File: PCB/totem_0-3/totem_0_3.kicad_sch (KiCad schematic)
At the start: 93 parts, among them J1 MJ-4PP-9, J2 MJ-4PP-9, J3 Conn_01x12_Socket, J4 Conn_01x03_Socket, SW1 SW_Push_45deg, SW10 SW_Push_45deg, SW11 SW_Push_45deg, SW12 SW_Push_45deg, SW13 SW_Push_45deg, SW14 SW_Push_45deg, SW15 SW_Push_45deg, SW16 SW_Push_45deg, SW17 SW_Push_45deg, SW18 SW_Push_45deg, SW19 SW_Push_45deg, SW2 SW_Push_45deg, SW20 SW_Push, SW21 SW_SPDT, SW22 SW_SPDT, SW23 SW_Push, SW24 SW_Push_45deg, SW25 SW_Push_45deg, SW26 SW_Push_45deg, SW27 SW_Push_45deg, SW28 SW_Push_45deg, SW29 SW_Push_45deg, SW3 SW_Push_45deg, SW30 SW_Push_45deg, SW31 SW_Push_45deg, SW32 SW_Push_45deg, SW33 SW_Push_45deg, SW34 SW_Push_45deg, SW35 SW_Push_45deg, SW36 SW_Push_45deg, SW37 SW_Push_45deg, SW38 SW_Push_45deg, SW39 SW_Push_45deg, SW4 SW_Push_45deg, SW40 SW_Push_45deg, SW41 SW_Push_45deg, SW42 SW_Push_45deg, SW5 SW_Push_45deg, SW6 SW_Push_45deg, SW7 SW_Push_45deg, SW8 SW_Push_45deg, SW9 SW_Push_45deg, U1 xiao-ble, U2 74HC595, U3 xiao-ble

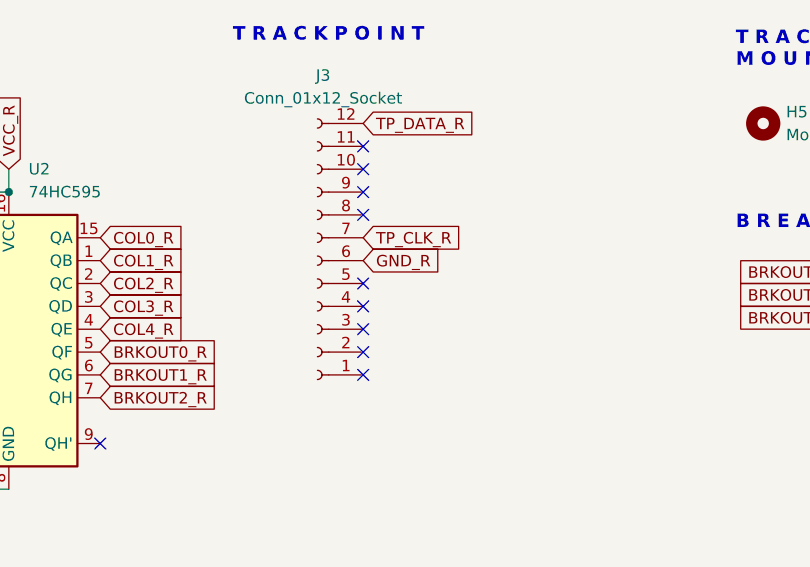
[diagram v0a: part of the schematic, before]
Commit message: sch: add VCC for trackpoint
Signed-off-by: Anant Thazhemadam <anant.thazhemadam@gmail.com>
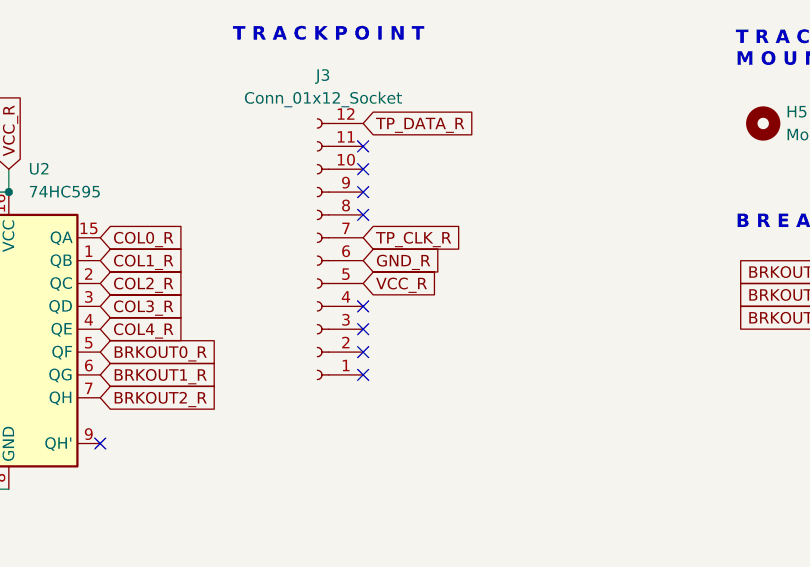
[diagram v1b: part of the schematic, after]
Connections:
- net VCC_R: now also J3.5 (Pin_5)
- no-connect marks 22 -> 21
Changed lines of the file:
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@@
-	)
-	(no_connect
-		(at 257.81 207.01)
 	)
 	(no_connect
@@
 			(effects
 				(font
+					(size 1.27 1.27)
+				)
+				(justify left)
+				(hide yes)
+			)
+		)
+	)
+	(global_label "VCC_R"
+		(shape input)
+		(at 257.81 207.01 0)
+		(fields_autoplaced yes)
+		(effects
+			(font
+				(size 1.27 1.27)
+			)
+			(justify left)
+		)
+		(property "Intersheetrefs" "${INTERSHEET_REFS}"
+			(at 266.0893 206.9306 0)
+			(effects
+				(font

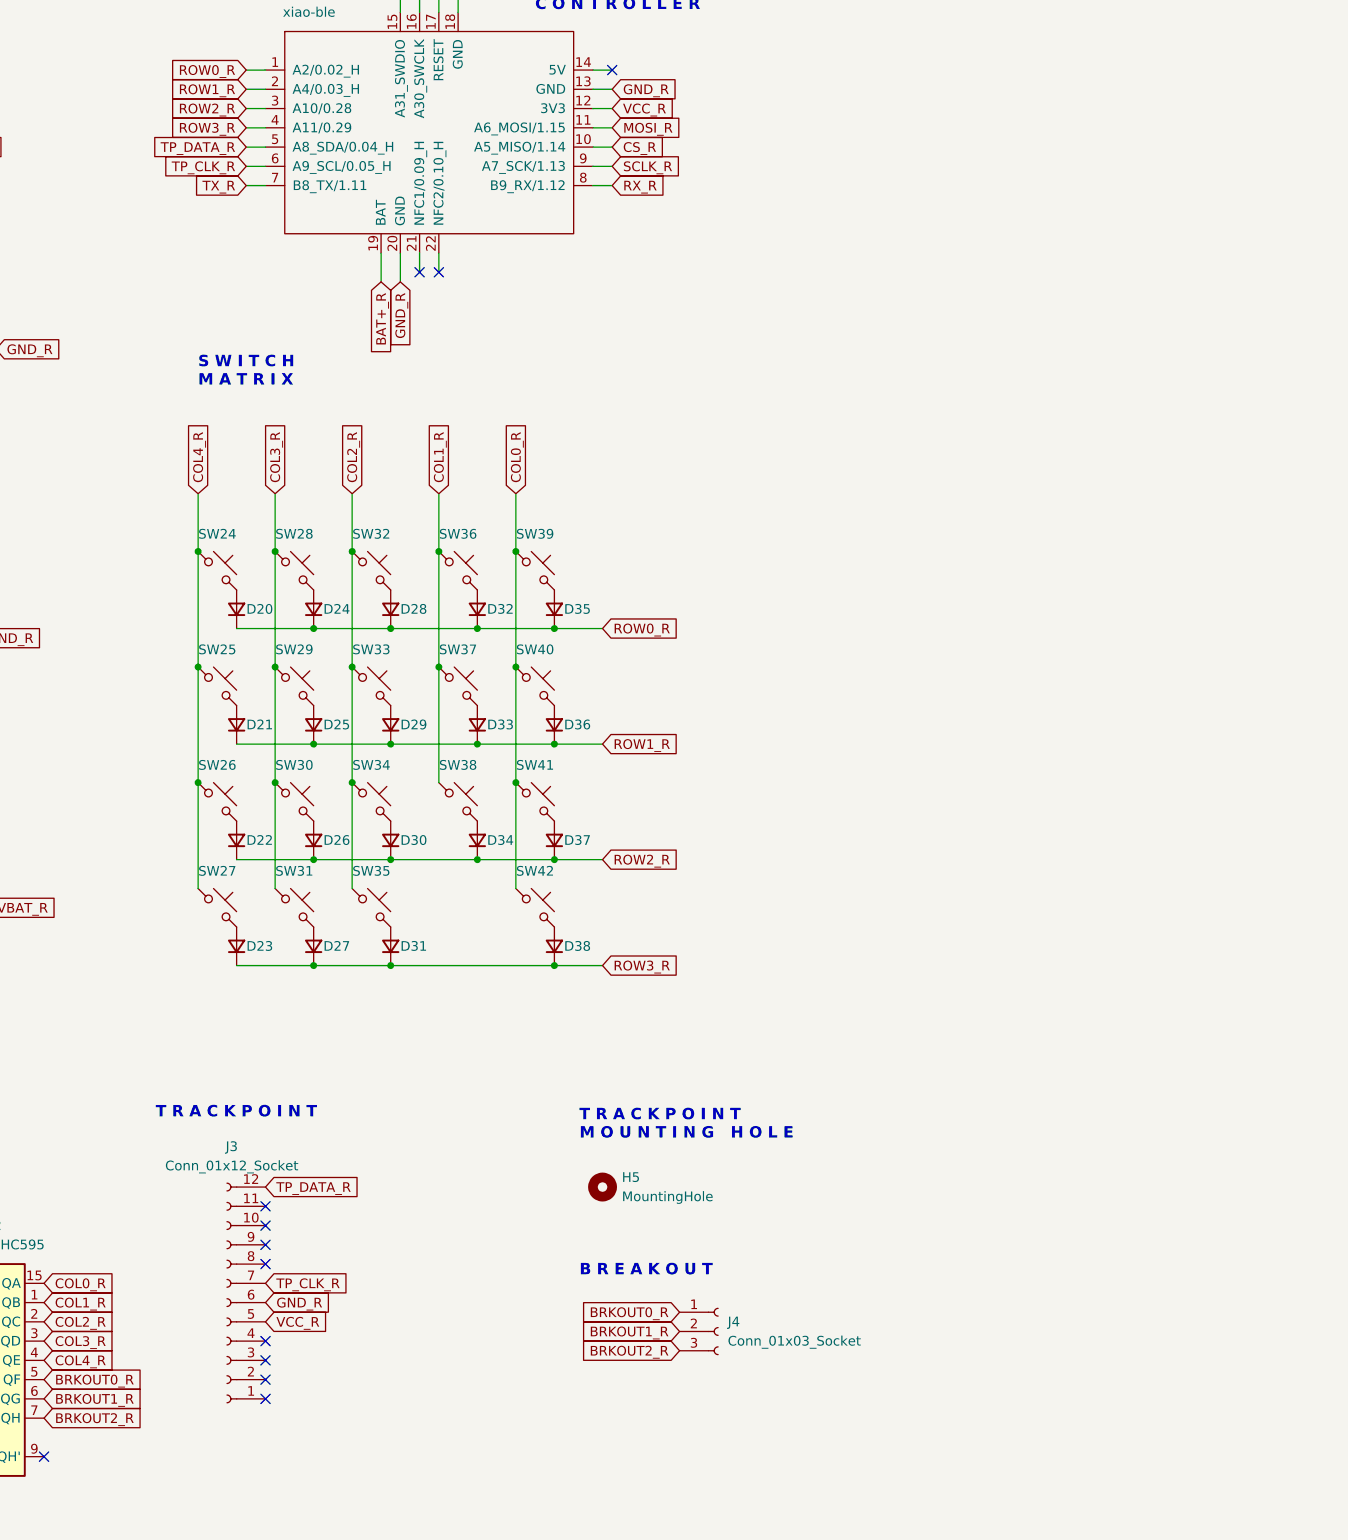
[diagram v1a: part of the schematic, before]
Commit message: sch: properly wire up trackpoint connector
Signed-off-by: Anant Thazhemadam <anant.thazhemadam@gmail.com>
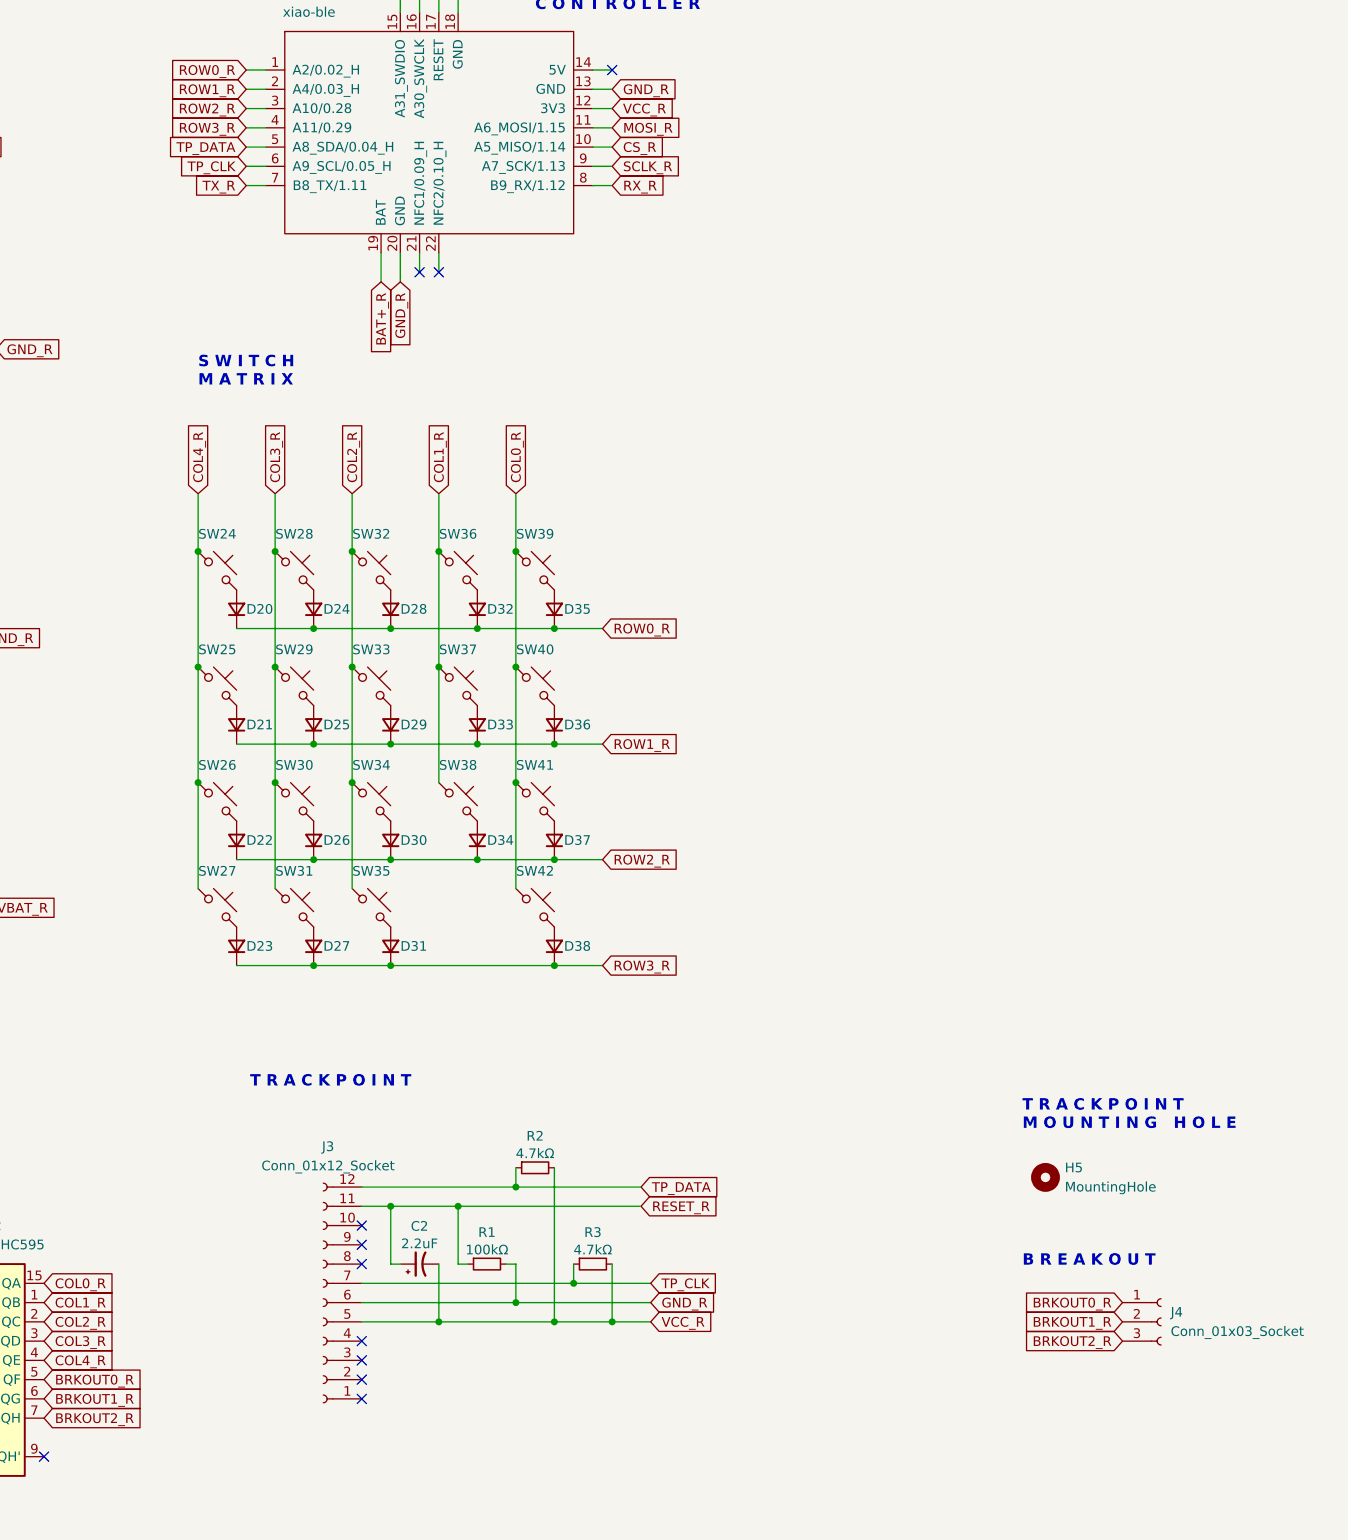
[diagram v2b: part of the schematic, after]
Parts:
- added C2: 2.2uF, Capacitor_SMD:C_0805_2012Metric_Pad1.18x1.45mm_HandSolder, symbol Device:CP1_Small
- added R1: 100kΩ, Resistor_SMD:R_0805_2012Metric_Pad1.20x1.40mm_HandSolder, symbol Device:R_Small
- added R2, R3: 4.7kΩ, Resistor_SMD:R_0805_2012Metric_Pad1.20x1.40mm_HandSolder, symbol Device:R_Small
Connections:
- net GND_R: now also R1.2
- net RESET_R: now also J3.11 (Pin_11), C2.1, R1.1
- net VCC_R: now also C2.2, R2.2, R3.2
- net TP_CLK_R renamed TP_CLK
- net TP_CLK: now also R3.1
- net TP_DATA_R renamed TP_DATA
- net TP_DATA: now also R2.1
- no-connect marks 21 -> 20
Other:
- moved on the sheet: H5, J3, J4

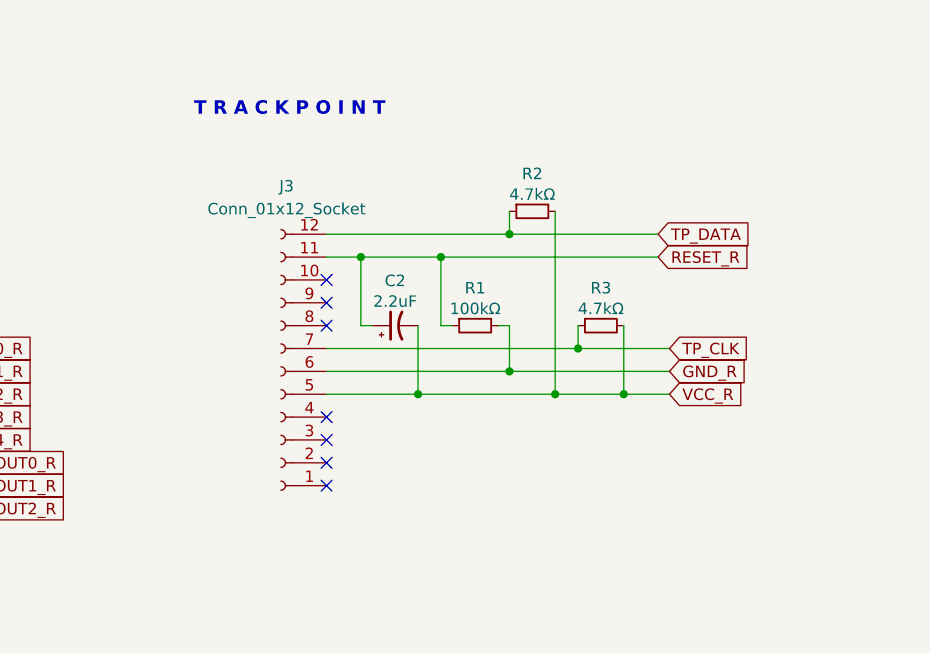
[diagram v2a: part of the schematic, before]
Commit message: sch: fix reset circuit for trackpoint
Signed-off-by: Anant Thazhemadam <anant.thazhemadam@gmail.com>
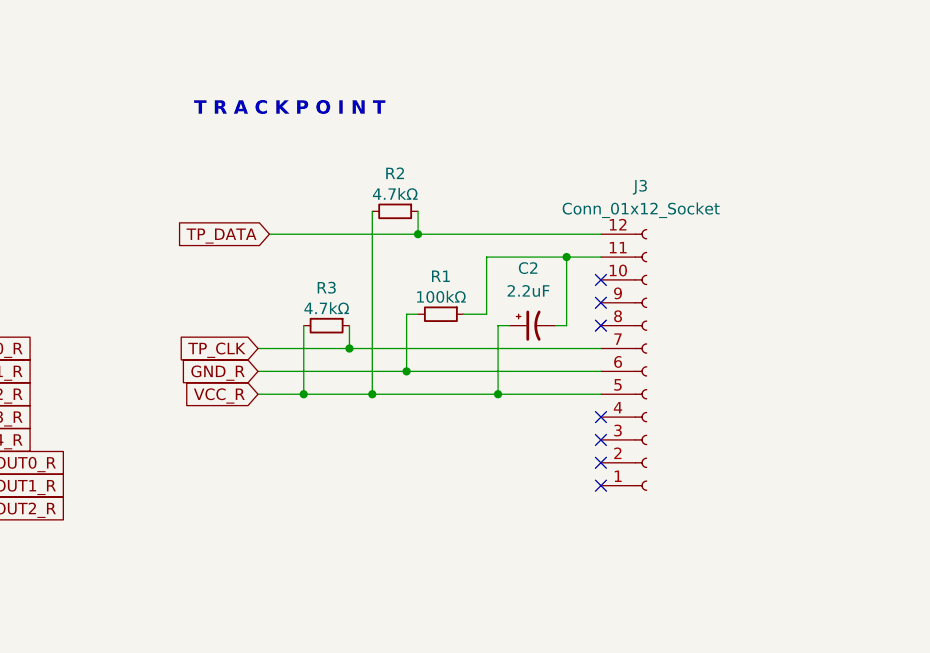
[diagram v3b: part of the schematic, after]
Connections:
- net RESET_R: no longer C2.1, J3.11 (Pin_11), R1.1
- net VCC_R: now also C2.1; no longer C2.2
- new net: C2.2, J3.11 (Pin_11), R1.1
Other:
- moved on the sheet: C2, J3, R1, R2, R3

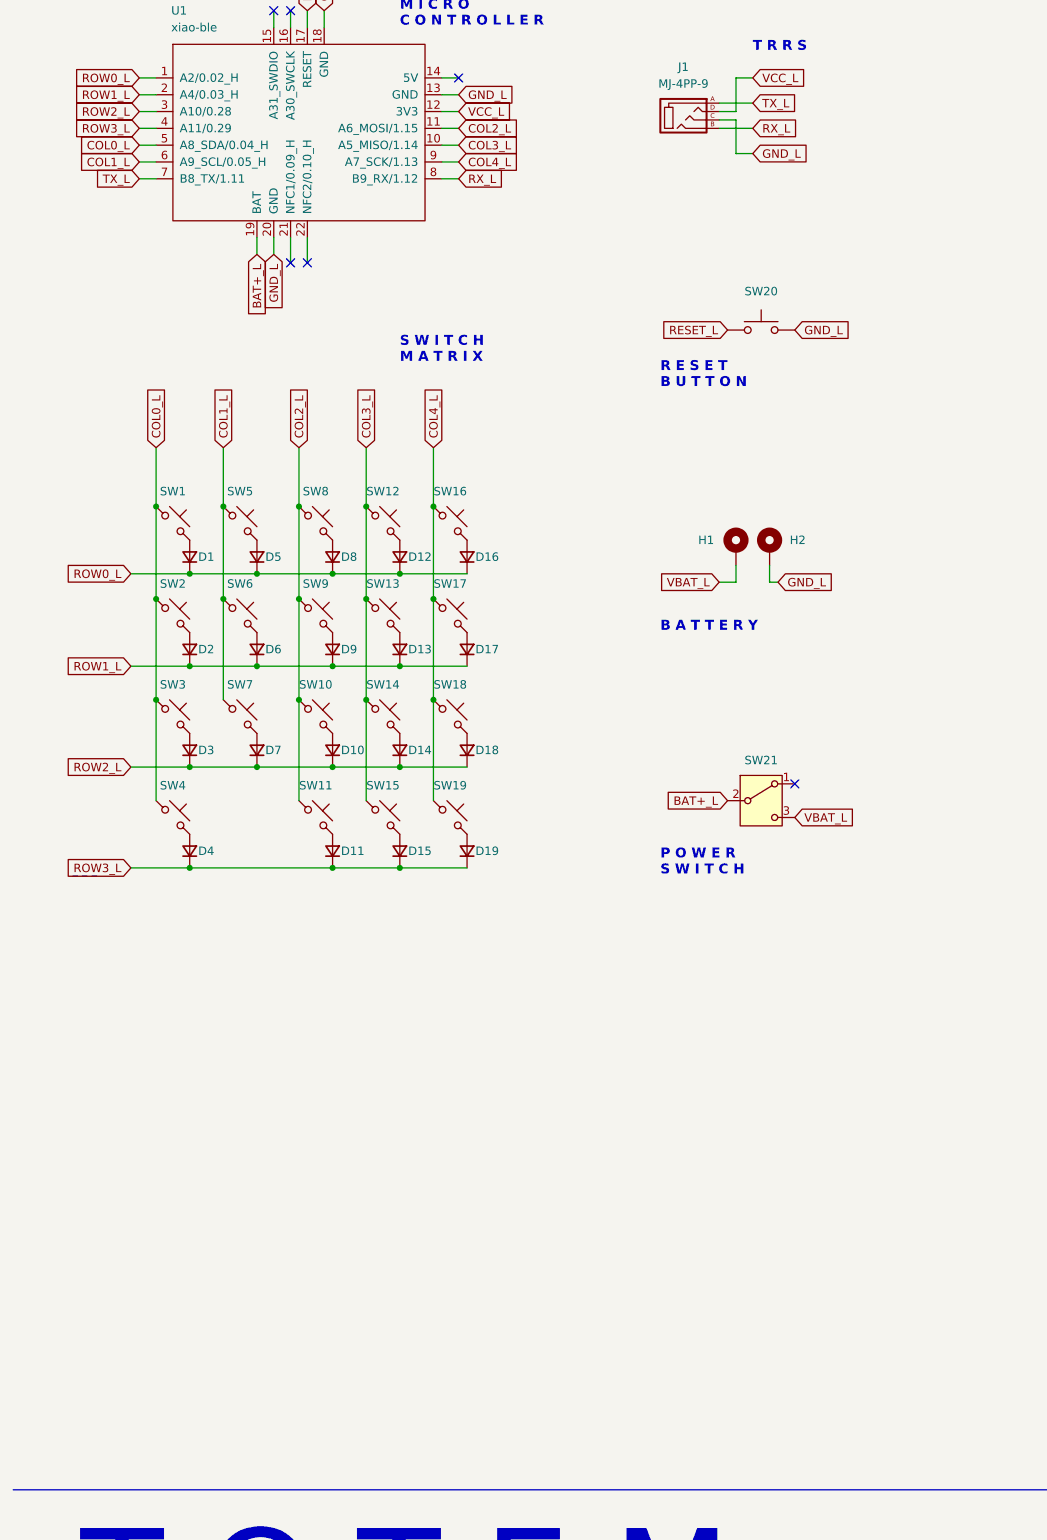
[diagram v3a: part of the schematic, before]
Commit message: sch: add shift register on lhs for electrical symmetry
Signed-off-by: Anant Thazhemadam <anant.thazhemadam@gmail.com>
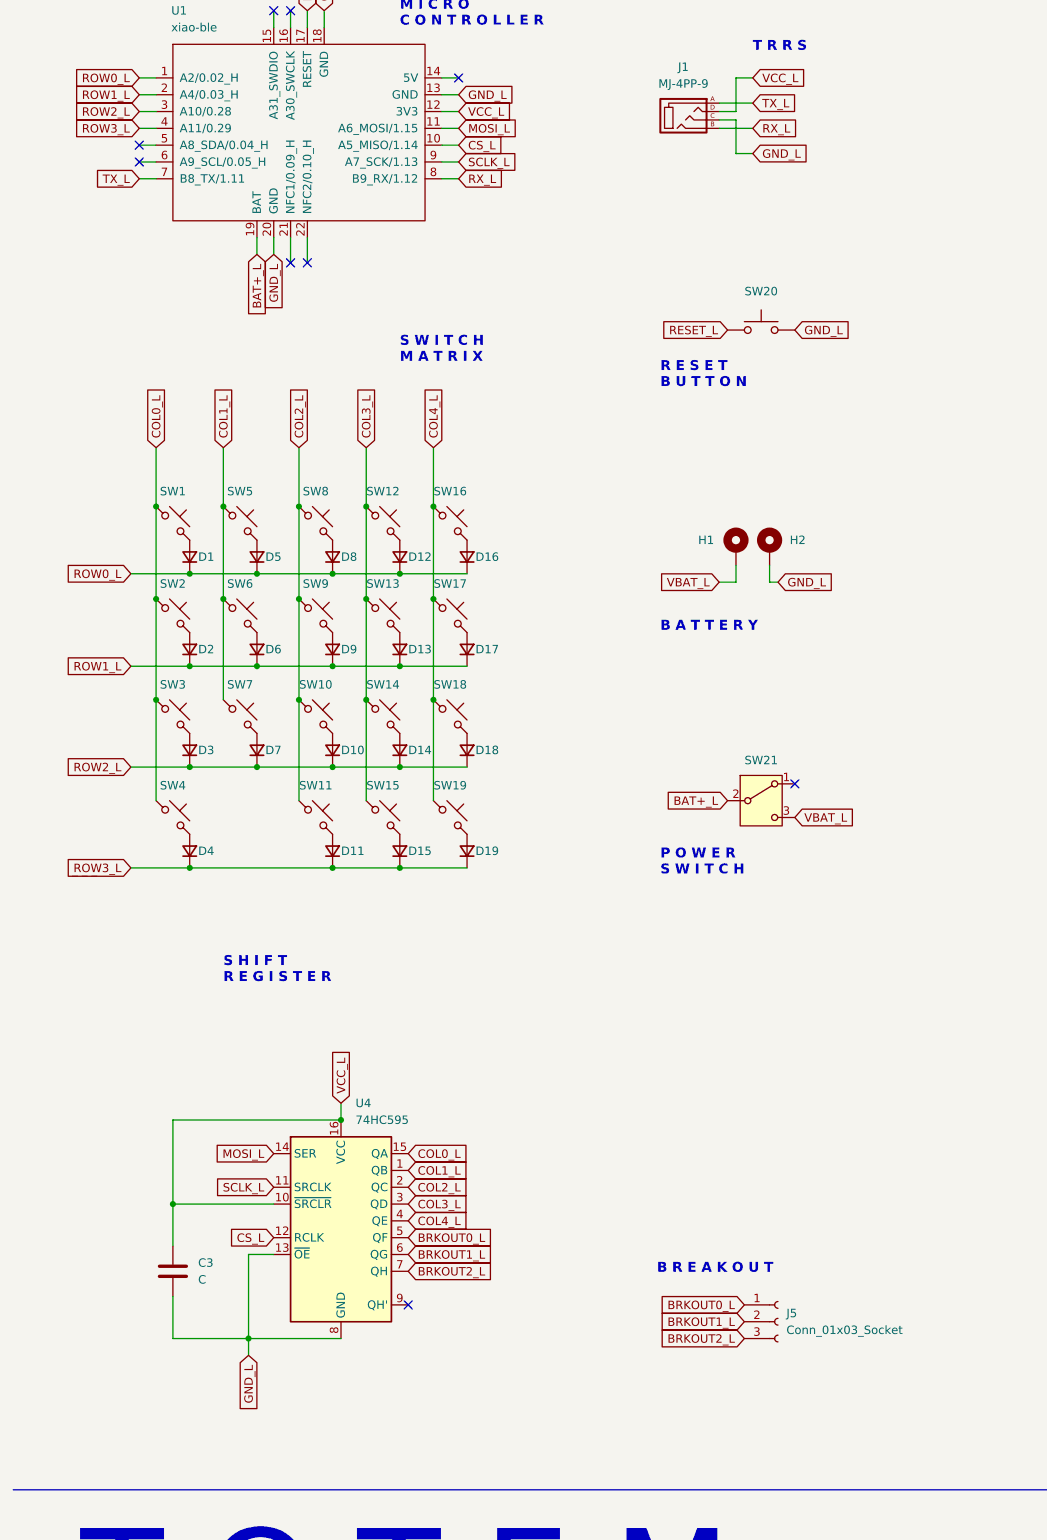
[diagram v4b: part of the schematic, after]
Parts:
- added C3: C, Capacitor_SMD:C_0805_2012Metric_Pad1.18x1.45mm_HandSolder, symbol Device:C
- added J5: Conn_01x03_Socket, Connector_PinHeader_2.54mm:PinHeader_1x03_P2.54mm_Vertical, symbol Connector:Conn_01x03_Socket
- added U4: 74HC595, Package_SO:SOIC-16_3.9x9.9mm_P1.27mm, symbol 74xx:74HC595
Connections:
- net COL0_L: now also U4.15 (QA); no longer U1.5 (A8_SDA/0.04_H)
- net COL1_L: now also U4.1 (QB); no longer U1.6 (A9_SCL/0.05_H)
- net COL2_L: now also U4.2 (QC); no longer U1.11 (A6_MOSI/1.15)
- net COL3_L: now also U4.3 (QD); no longer U1.10 (A5_MISO/1.14)
- net COL4_L: now also U4.4 (QE); no longer U1.9 (A7_SCK/1.13)
- net GND_L: now also C3.2, U4.13 (~{OE}), U4.8 (GND)
- net VCC_L: now also C3.1, U4.10 (~{SRCLR}), U4.16 (VCC)
- new net BRKOUT0_L: J5.1 (Pin_1), U4.5 (QF)
- new net BRKOUT1_L: J5.2 (Pin_2), U4.6 (QG)
- new net BRKOUT2_L: J5.3 (Pin_3), U4.7 (QH)
- new net CS_L: U1.10 (A5_MISO/1.14), U4.12 (RCLK)
- new net MOSI_L: U1.11 (A6_MOSI/1.15), U4.14 (SER)
- new net SCLK_L: U1.9 (A7_SCK/1.13), U4.11 (SRCLK)
- no-connect marks 20 -> 23
